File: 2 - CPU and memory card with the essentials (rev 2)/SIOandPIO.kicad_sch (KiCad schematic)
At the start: 21 parts, among them J10 RX BUS DIS, J11 TX BUS DIS, J3 SIO CLK, J4 COM1: DCE, J5 RTS/CTR DIR, J6 VCC DIS, J7 COM2: TTL, J8 DATA DIR, J9 DTR|RTS/CTS, U12 Z84C3010 CTC, U13 MAX232, U14 Z84C4010

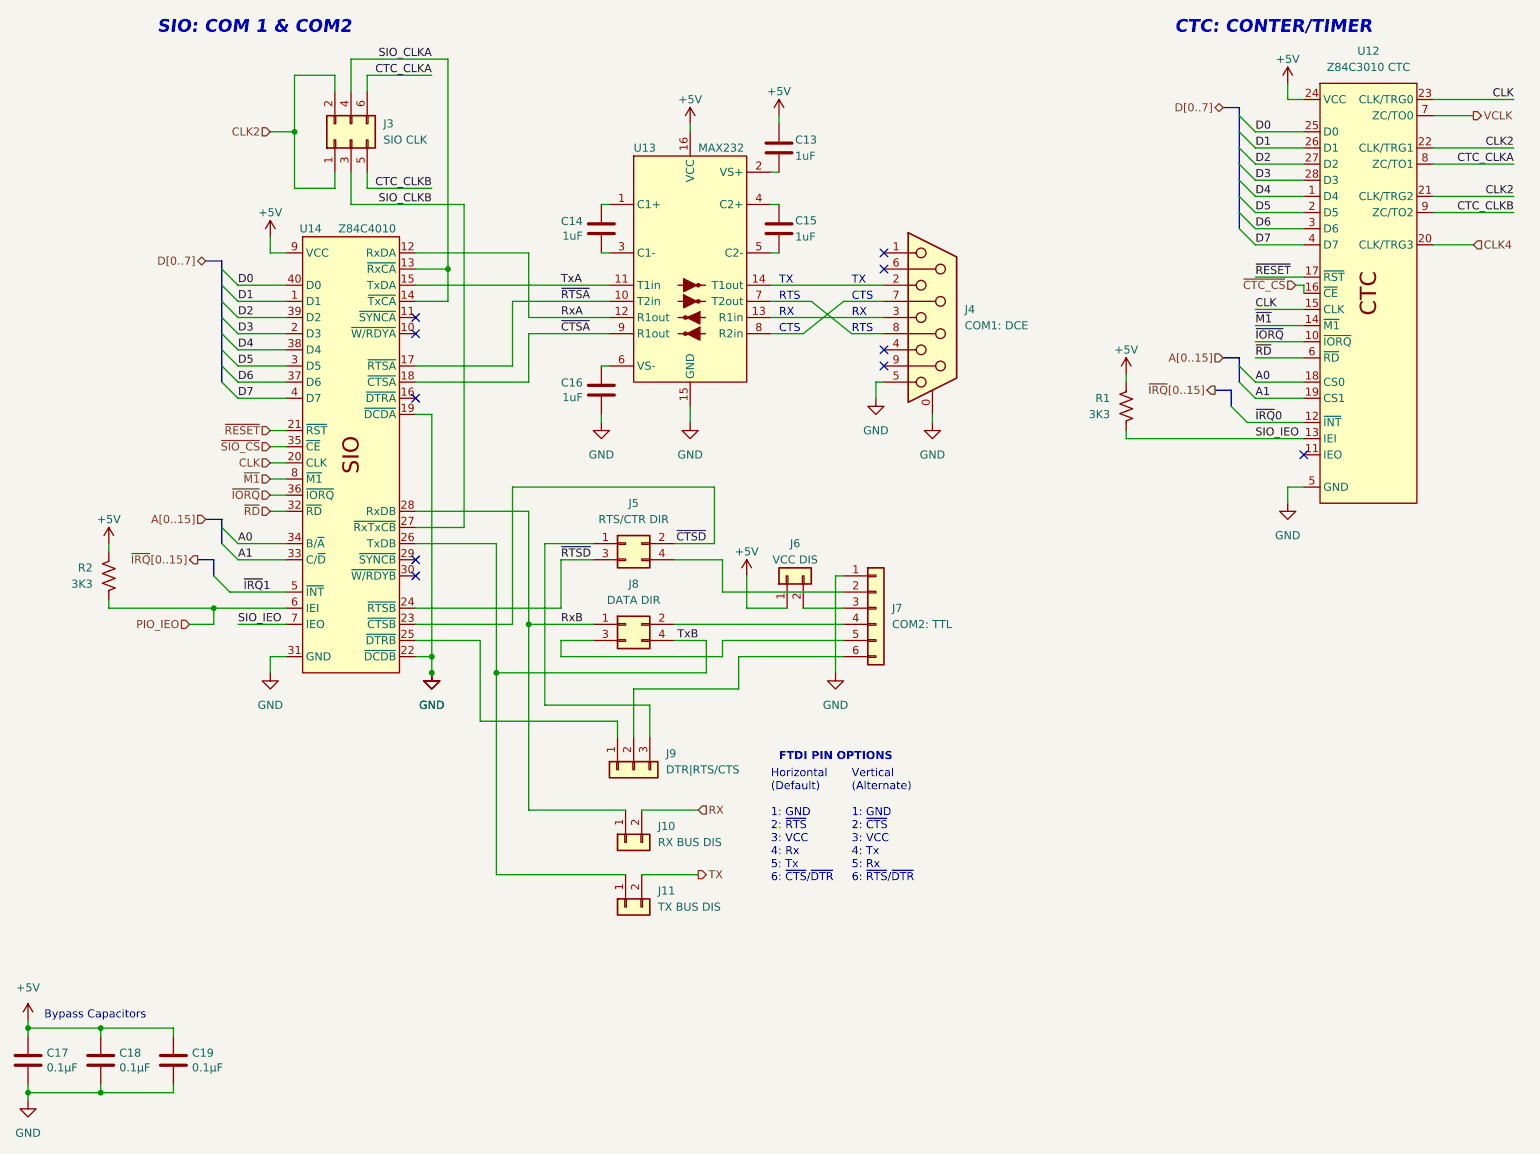
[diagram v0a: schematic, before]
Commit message: Updated disk activity circuit in mother board, and improved layout in CPU card
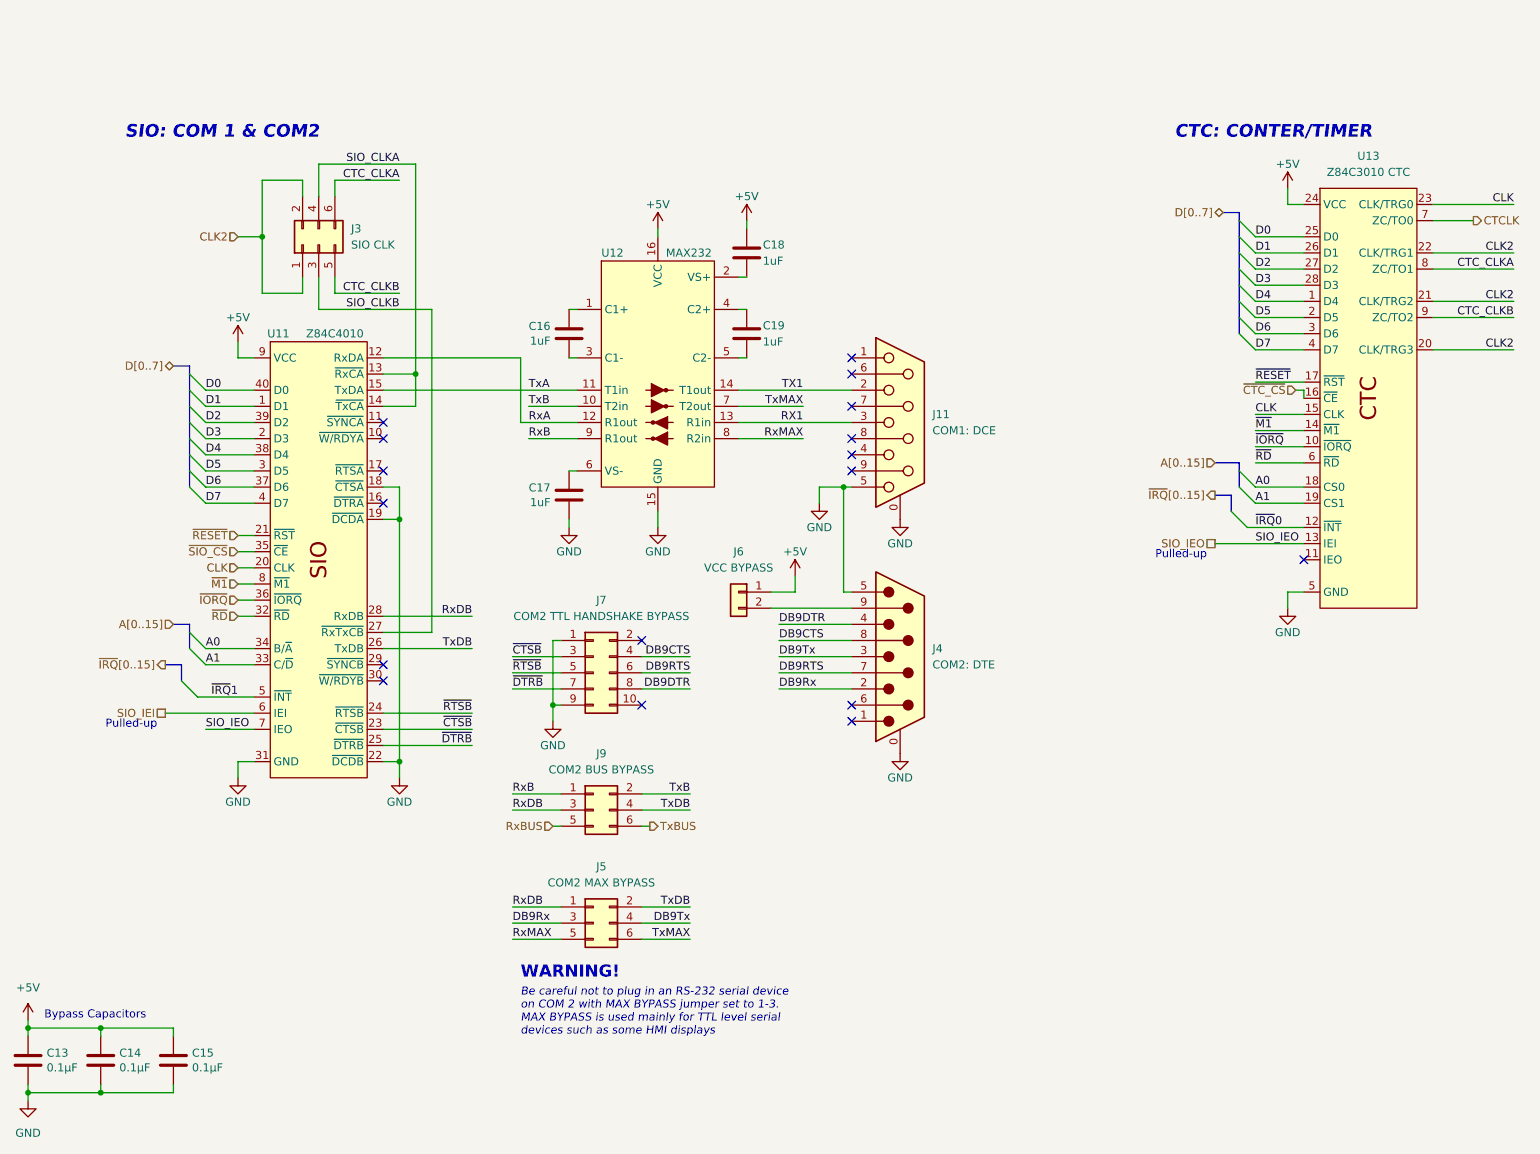
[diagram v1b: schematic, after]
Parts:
- removed J10: RX BUS DIS, Connector_PinHeader_2.54mm:PinHeader_1x02_P2.54mm_Vertical, symbol Connector_Generic:Conn_01x02
- removed J11: TX BUS DIS, Connector_PinHeader_2.54mm:PinHeader_1x02_P2.54mm_Vertical, symbol Connector_Generic:Conn_01x02
- removed J5: RTS/CTR DIR, Connector_PinHeader_2.54mm:PinHeader_2x02_P2.54mm_Vertical, symbol Connector_Generic:Conn_02x02_Odd_Even
- removed J7: COM2: TTL, Connector_PinHeader_2.54mm:PinHeader_1x06_P2.54mm_Horizontal, symbol Connector_Generic:Conn_01x06
- removed J8: DATA DIR, Connector_PinHeader_2.54mm:PinHeader_2x02_P2.54mm_Vertical, symbol Connector_Generic:Conn_02x02_Odd_Even
- removed J9: DTR|RTS/CTS, Connector_PinHeader_2.54mm:PinHeader_1x03_P2.54mm_Vertical, symbol Connector_Generic:Conn_01x03
- removed R1, R2: 3K3, Resistor_THT:R_Axial_DIN0207_L6.3mm_D2.5mm_P10.16mm_Horizontal, symbol Device:R_US
- added J4: COM2: DTE, Connector_Dsub:DSUB-9_Male_Horizontal_P2.77x2.84mm_EdgePinOffset4.94mm_Housed_MountingHolesOffset7.48mm, symbol Connector:DE9_Plug_MountingHoles
- added J5: COM2 MAX BYPASS, Connector_PinHeader_2.54mm:PinHeader_2x03_P2.54mm_Vertical, symbol Connector_Generic:Conn_02x03_Odd_Even
- added J7: COM2 TTL HANDSHAKE BYPASS, Connector_PinHeader_2.54mm:PinHeader_2x05_P2.54mm_Vertical, symbol Connector_Generic:Conn_02x05_Odd_Even
- added J9: COM2 BUS BYPASS, Connector_PinHeader_2.54mm:PinHeader_2x03_P2.54mm_Vertical, symbol Connector_Generic:Conn_02x03_Odd_Even
- J6: value VCC DIS -> VCC BYPASS
- renumbered C17 to C13, C18 to C14, C19 to C15, C14 to C16, C16 to C17, C13 to C18, C15 to C19, J4 to J11, U14 to U11, U13 to U12, U12 to U13
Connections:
- net CLK4 is gone; now on net CLK2: U13.20 (CLK/TRG3)
- net GND: now also U11.18 (~{CTSA}), J4.0 (PAD), J4.5, J7.1 (Pin_1), J7.9 (Pin_9)
- net RxB: now also U12.9 (R1out), J9.1 (Pin_1); no longer U11.28 (RxDB)
- net TxB: now also U12.10 (T2in), J9.2 (Pin_2); no longer U11.26 (TxDB)
- net RX1: now reaches J11.3, U12.13 (R1in)
- net TX1: now reaches J11.2, U12.14 (T1out)
- net at J11.8: no longer U12.7 (T2out)
- net at J11.7: no longer U12.8 (R2in)
- net ~{DTRB}: now reaches U11.25 (~{DTRB})
- net ~{DTRB}: now also J7.7 (Pin_7)
- net at J6.2 (Pin_2): now also J4.9
- net PIO_IEO renamed SIO_IEI
- net VCLK renamed CTCLK
- removed net ~{CTSA}: U11.18 (~{CTSA}), U12.9 (R1out)
- net ~{CTSD} renamed ~{CTSB}
- net ~{CTSB}: now also J7.3 (Pin_3)
- net ~{RTSA}: no longer names the net of U11.17 (~{RTSA})
- net ~{RTSA}: no longer U12.10 (T2in)
- net ~{RTSD} renamed ~{RTSB}
- net ~{RTSB}: now also J7.5 (Pin_5)
- new net DB9CTS: J4.8, J7.4 (Pin_4)
- new net DB9DTR: J4.4, J7.8 (Pin_8)
- new net DB9RTS: J4.7, J7.6 (Pin_6)
- new net DB9Rx: J4.2, J5.3 (Pin_3)
- new net DB9Tx: J4.3, J5.4 (Pin_4)
- new net RxBUS: J9.5 (Pin_5)
- new net RxDB: J5.1 (Pin_1), J9.3 (Pin_3), U11.28 (RxDB)
- new net RxMAX: J5.5 (Pin_5), U12.8 (R2in)
- new net TxBUS: J9.6 (Pin_6)
- new net TxDB: J5.2 (Pin_2), J9.4 (Pin_4), U11.26 (TxDB)
- new net TxMAX: J5.6 (Pin_6), U12.7 (T2out)
- no-connect marks 10 -> 17
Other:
- note added: "Be careful not to plug in an RS-232 serial device on COM 2 with MAX BYPASS jumper set to 1-3. MAX BYPASS is used mainly for TTL level serial devices such as some HMI displays"
- note added: "Pulled-up"
- note added: "WARNING!"
- note removed: "CTS"
- note removed: "FTDI PIN OPTIONS"
- note removed: "Horizontal (Default) 1: GND 2: ~{RTS} 3: VCC 4: Rx 5: Tx 6: ~{CTS}/~{DTR}"
- note removed: "RTS"
- note removed: "RX"
- note removed: "TX"
- note removed: "Vertical (Alternate) 1: GND 2: ~{CTS} 3: VCC 4: Tx 5: Rx 6: ~{RTS}/~{DTR}"
- title: (none) -> CTC and SIO
- moved on the sheet: C16, C17, C18, C19, J11, J3, U11, U12, U13
